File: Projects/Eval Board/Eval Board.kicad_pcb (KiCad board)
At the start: 2 copper layers, 50.8 x 33.5 mm, 34 parts, among them J1 I OUT, J2 Q OUT, J3 LO, J4 RF, U1 LTC5584

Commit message: Version 2
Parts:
- added J6: Conn_01x02, Connector_PinHeader_1.00mm:PinHeader_1x02_P1.00mm_Vertical, F.Cu at (175.9, 70.1)
- added J7: Conn_01x04, Connector_PinHeader_1.00mm:PinHeader_1x04_P1.00mm_Vertical, F.Cu at (200.7, 86.9)
- added J8: Conn_01x05, Connector_PinHeader_1.00mm:PinHeader_1x05_P1.00mm_Vertical, F.Cu at (182.9, 74.2)
- J1: value I OUT -> LO; footprint Kevin Library:SAMTEC_SMA-J-P-H-ST-EM1 -> AdditionalLibs:SAMTEC_SMA-J-P-H-ST-EM1
- J2: footprint Kevin Library:SAMTEC_SMA-J-P-H-ST-EM1 -> AdditionalLibs:SAMTEC_SMA-J-P-H-ST-EM1
- J3: value LO -> I Out; footprint Kevin Library:SAMTEC_SMA-J-P-H-ST-EM1 -> AdditionalLibs:SAMTEC_SMA-J-P-H-ST-EM1
- J4: value RF -> Q OUT; footprint Kevin Library:SAMTEC_SMA-J-P-H-ST-EM1 -> AdditionalLibs:SAMTEC_SMA-J-P-H-ST-EM1
- moved J1 32.7 mm to (217.6, 82.5), turned to 90 degrees
- moved J3 31.1 mm to (193.5, 67.3), turned to 180 degrees
- moved C21 18.4 mm to (196.6, 75.7), turned to 0 degrees
- moved C30 12.2 mm to (208.5, 75.7), turned to 0 degrees
- moved R14 5.77 mm to (206.8, 73.4)
- moved C35 5.39 mm to (183.9, 80.3), turned to 0 degrees
- moved C29 4.81 mm to (186.7, 73.7), turned to 180 degrees
- moved R9 4.67 mm to (190.0, 73.7)
- moved C41 4.34 mm to (191.0, 85.1)
- moved C19 4.06 mm to (182.9, 84.3)
- moved J2 3.86 mm to (207.0, 67.3)
- moved C31 3.07 mm to (193.0, 79.0)
- moved TR2 2.81 mm to (186.4, 84.8)
- moved L5 2.75 mm to (210.6, 82.5)
- moved C17 2.65 mm to (178.1, 84.3)
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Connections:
- net DCOI renamed /DCOI
- net DCOQ renamed /DCOQ
- net IP2I renamed /IP21
- net IP2Q renamed /IP2Q
- net Net-(C17-Pad1) renamed /RF
- net Net-(J2-Pad1) renamed /Q+
- net Net-(J2-Pad2_1) renamed /Q-
- C14 pad 1: Net-(C14-Pad1) -> /LO
- J1 pad 1: Net-(J1-Pad1) -> /LO
- J1 pad 2_1: Net-(J1-Pad2_1) -> GND
- J1 pad 2_2: Net-(J1-Pad2_1) -> GND
- J1 pad 3_1: Net-(J1-Pad2_1) -> GND
- J1 pad 3_2: Net-(J1-Pad2_1) -> GND
- J3 pad 1: Net-(C14-Pad1) -> /I+
- J3 pad 2_1: GND -> /I-
- J3 pad 2_2: GND -> /I-
- J3 pad 3_1: GND -> /I-
- J3 pad 3_2: GND -> /I-
- L5 pad 2: Net-(C14-Pad1) -> /LO
- R11 pad 1: Net-(J1-Pad1) -> /I+
- R9 pad 1: Net-(J1-Pad2_1) -> /I-
- U1 pad 22: Net-(J1-Pad1) -> /I+
- U1 pad 23: Net-(J1-Pad2_1) -> /I-
- U1 pad 25: (no net) -> GND
- U1 pad 9: Net-(U1-Pad9) -> Vbias
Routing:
- net GND: track 61.1 -> 10.5 mm, vias 169 -> 161
- net VCC: track 99.5 -> 61.3 mm, vias 4 -> 8
- net Net-(J1-Pad1): track 23.1 -> 0.00 mm
- net Net-(J1-Pad2_1): track 22.8 -> 0.00 mm, vias 18 -> 0
- net /I-: track 0.00 -> 13.4 mm, vias 0 -> 8
- net /I+: track 0.00 -> 12.6 mm
- net Net-(C14-Pad1): track 12.2 -> 0.00 mm
- net EN: track 0.00 -> 11.3 mm
- net Vbias: track 0.00 -> 10.5 mm
- net /Q+: track 25.7 -> 19.1 mm
- net /LO: track 0.00 -> 6.20 mm
- net EDC: track 0.00 -> 5.97 mm
- net /Q-: track 27.6 -> 21.6 mm, vias 40 -> 8
- net EIP2: track 0.00 -> 4.80 mm
- net /DCOI: track 10.1 -> 13.3 mm, vias 1 -> 0
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- added copper zone on B.Cu, net /I-
- added copper zone on F.Cu, net /I-
- added copper zone on B.Cu, net VCC
- removed copper zone on B.Cu, net Net-(J1-Pad2_1)
- removed copper zone on F.Cu, net Net-(J1-Pad2_1)
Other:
- board size 50.8 x 33.5 mm -> 48.3 x 27.3 mm
- board text removed: "GTRF Mixer Eval Board Rev 0.1"

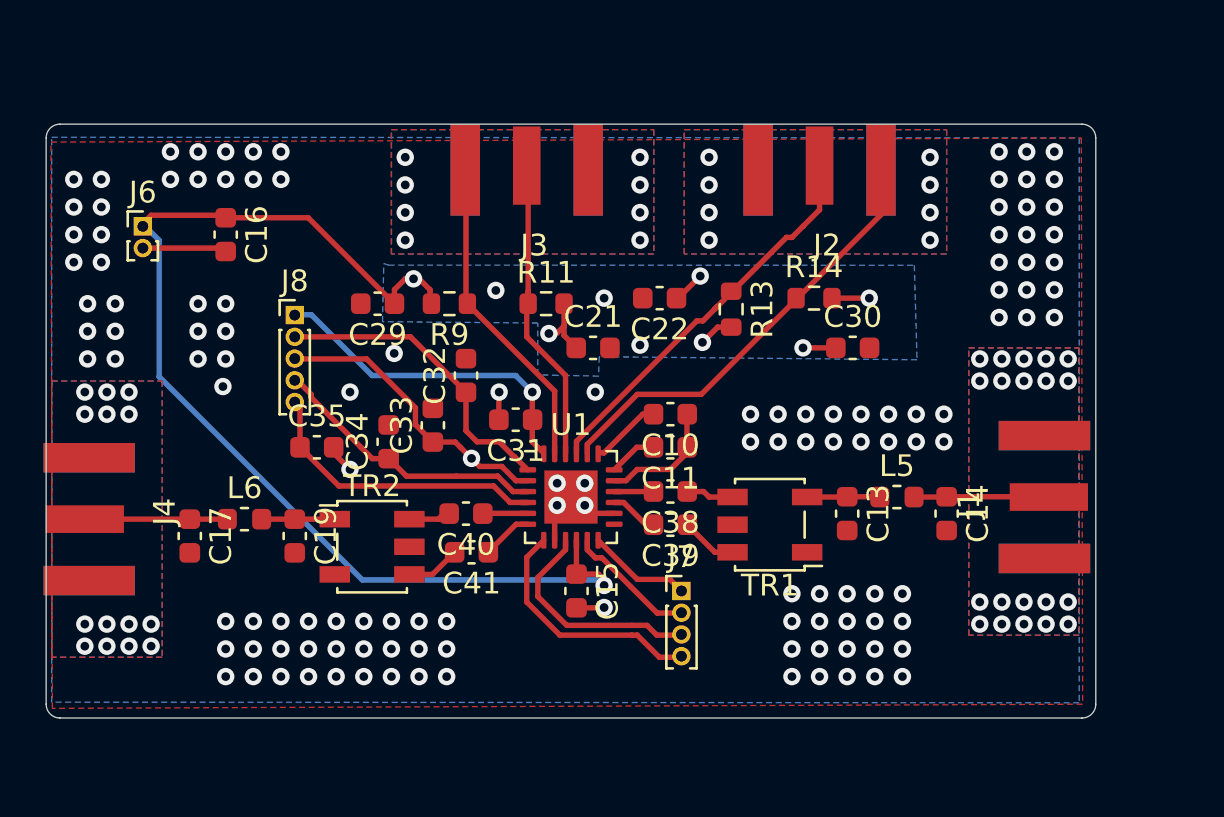
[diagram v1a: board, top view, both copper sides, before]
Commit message: Adjusted the VCC trace on the mixer eval board
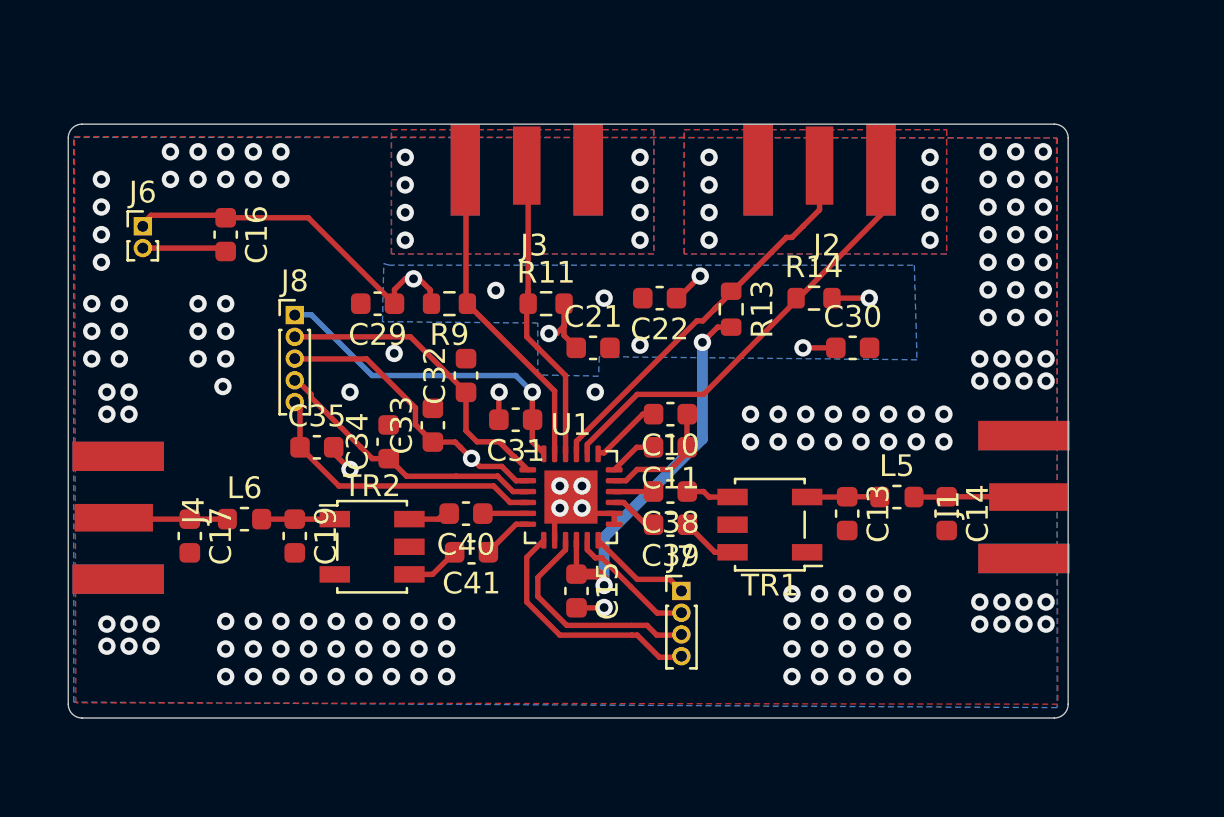
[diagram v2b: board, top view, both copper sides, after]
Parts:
- moved J4 1.34 mm to (174.6, 83.5)
- moved J1 0.94 mm to (216.6, 82.5)
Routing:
- net VCC: track 61.3 -> 42.8 mm
- net GND: track 10.5 -> 11.0 mm, vias 161 -> 149
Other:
- board size 48.3 x 27.3 mm -> 46 x 27.3 mm

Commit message: I made a 4 layer variant of the mixer PCB
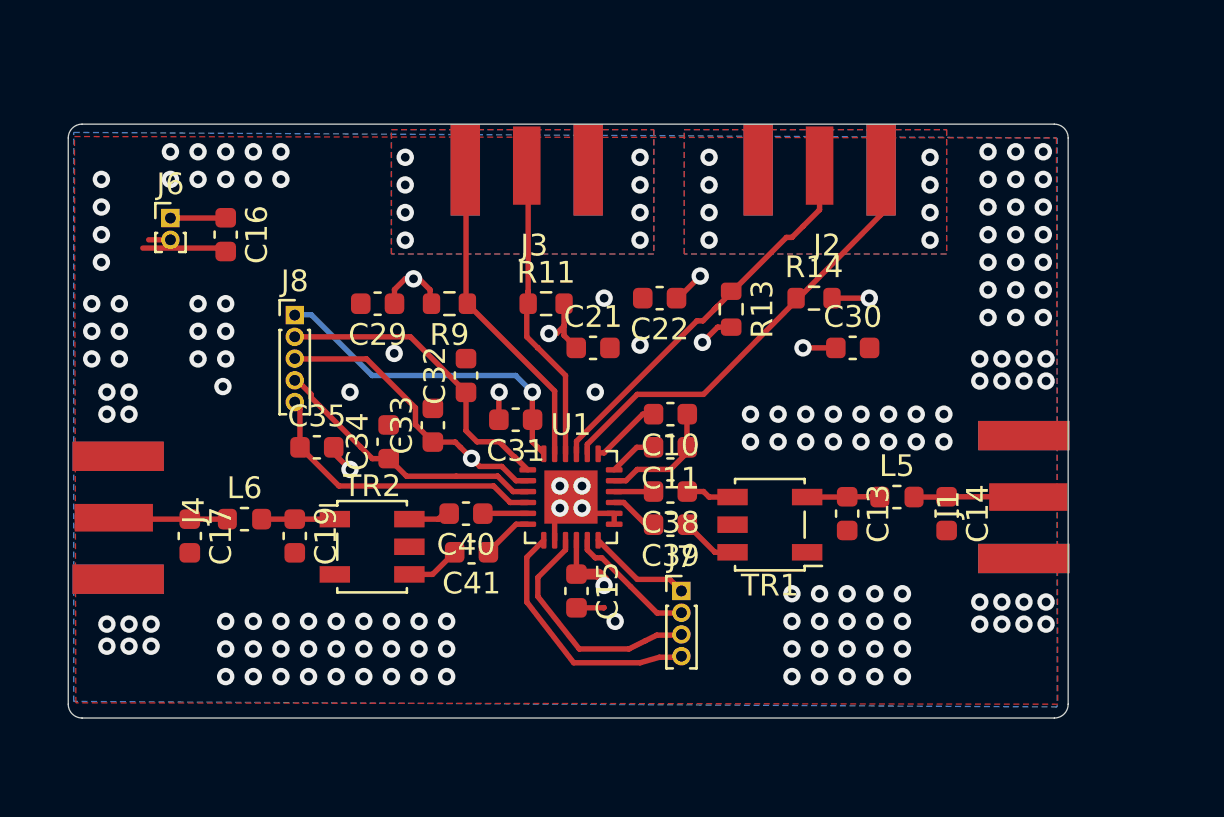
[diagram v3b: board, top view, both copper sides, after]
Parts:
- moved J6 1.33 mm to (177.2, 69.7)
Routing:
- net VCC: track 42.8 -> 19.0 mm, vias 8 -> 7
- net GND: track 11.0 -> 12.0 mm
- net Vbias: track 10.5 -> 11.0 mm
- added copper zone on In1.Cu, net GND
- added copper zone on In2.Cu, net VCC
- removed copper zone on B.Cu, net VCC
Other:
- copper layers 2 -> 4
- rule via_min_drill: 0.3 -> 0.2
- rule via_min_size: 0.4 -> 0.3

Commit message: Fixed DRC error on the jumpers
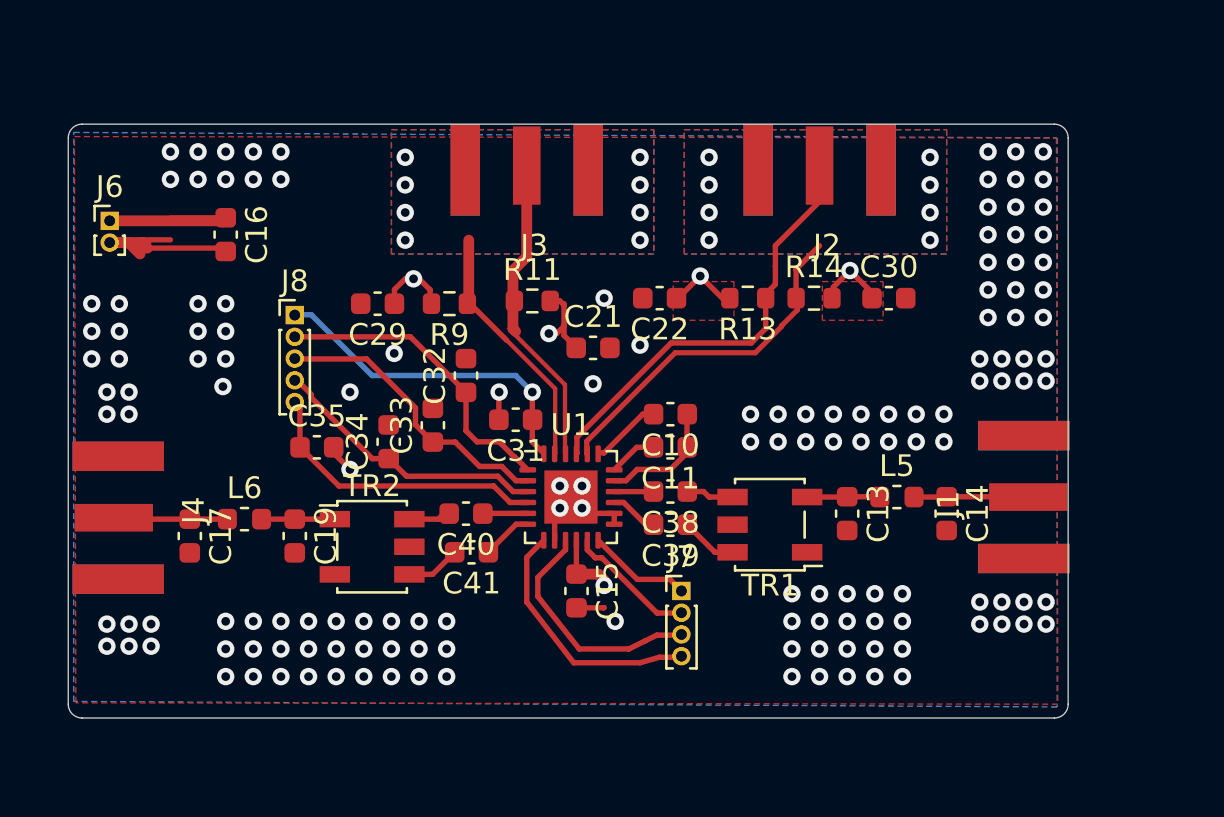
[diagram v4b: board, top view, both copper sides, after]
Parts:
- moved C30 2.83 mm to (210.2, 73.4)
- moved J6 2.80 mm to (174.4, 69.8)
- moved R13 0.92 mm to (203.7, 73.4), turned to 180 degrees
- moved R11 0.65 mm to (193.8, 73.5)
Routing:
- net VCC: track 19.0 -> 25.4 mm, vias 7 -> 5
- net /Q-: track 21.7 -> 16.2 mm
- net GND: track 12.0 -> 15.6 mm, vias 149 -> 145
- net /I-: track 13.4 -> 11.5 mm
- net /I+: track 12.6 -> 14.5 mm
- net /Q+: track 19.1 -> 20.3 mm
- net /DCOQ: vias 1 -> 0
- added copper zone on F.Cu, net VCC

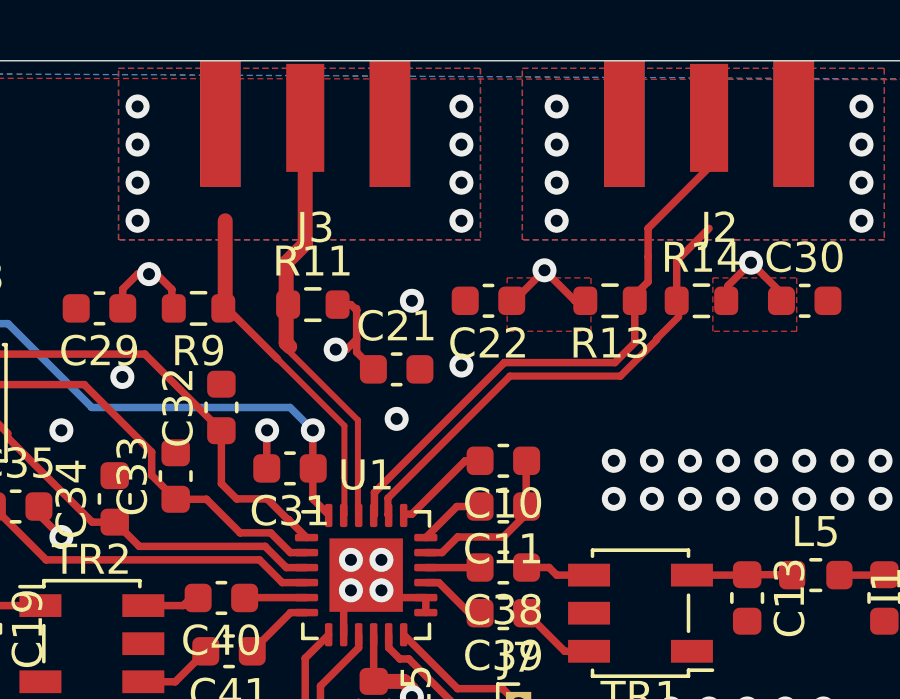
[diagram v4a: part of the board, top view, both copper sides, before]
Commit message: I tried to route diff pairs a little better on this one but they're still not good
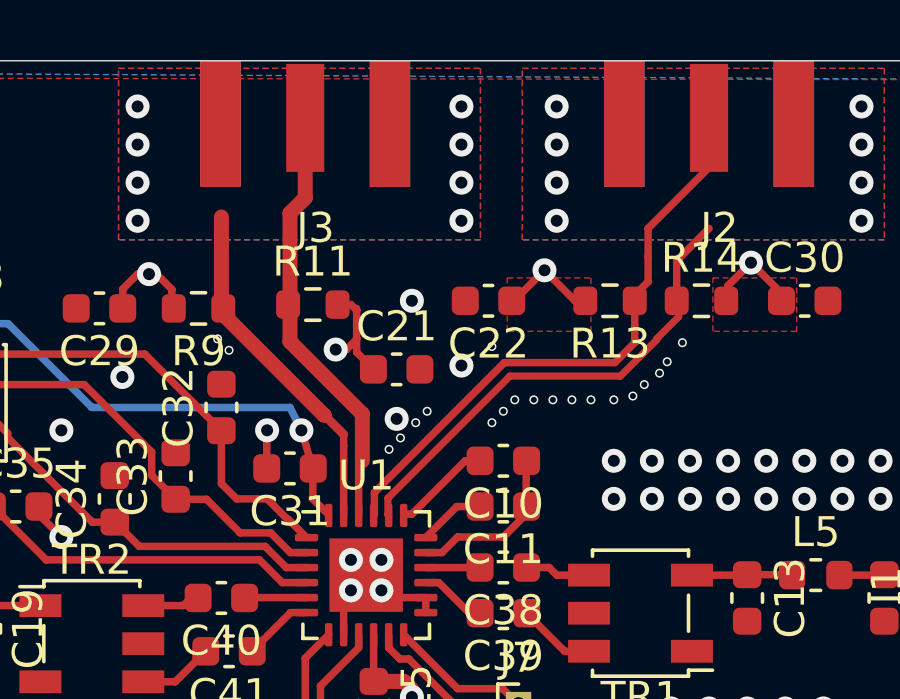
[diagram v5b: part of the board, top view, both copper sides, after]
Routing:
- net /I+: track 14.5 -> 15.3 mm
- net GND: vias 145 -> 165
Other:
- net class Dpair added: clearance 0.2, trace_width 0.25, via_dia 0.8, via_drill 0.4

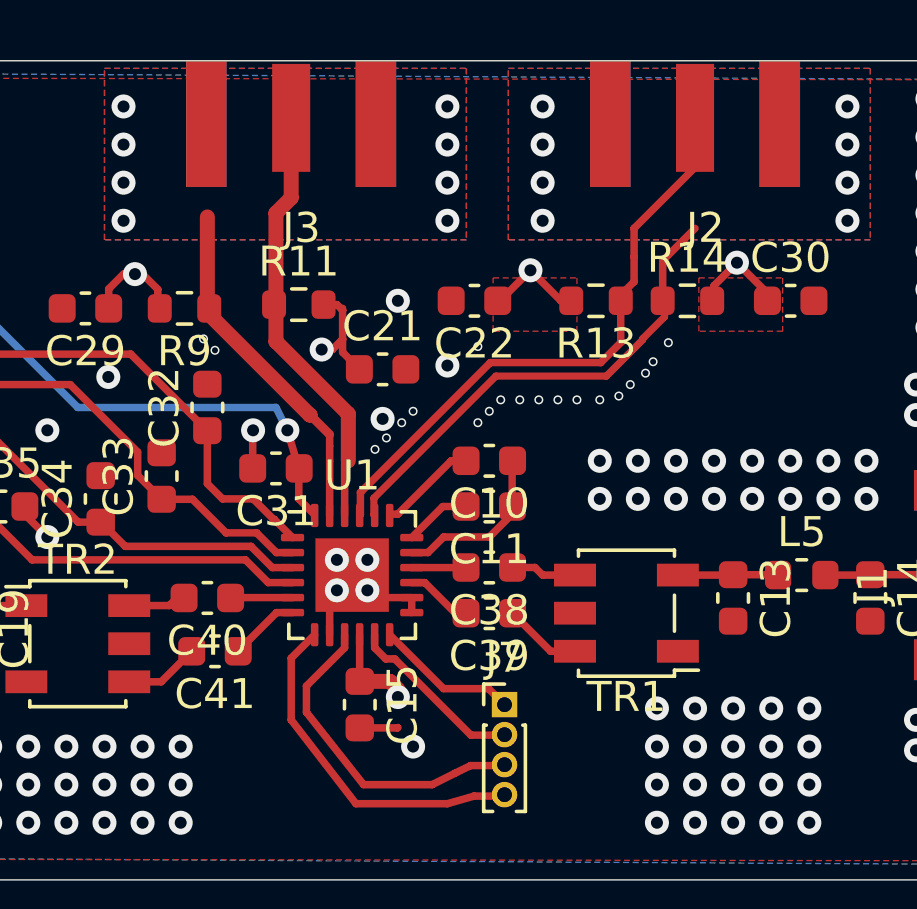
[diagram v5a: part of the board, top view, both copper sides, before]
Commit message: adjusted trace width on I+/- and Q+/- to reduce inductance. The traces are not drawn as duplex
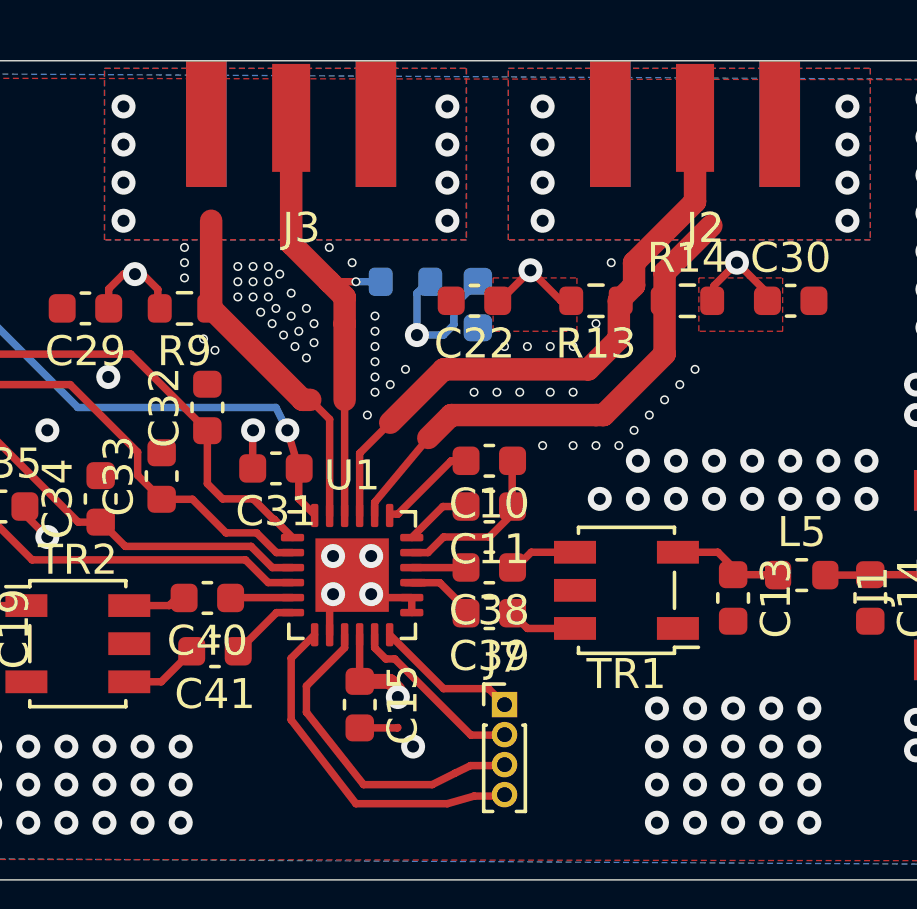
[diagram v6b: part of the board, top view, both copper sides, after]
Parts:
- C21, R11: moved to B.Cu
- moved C21 3.84 mm to (199.8, 73.5), turned to 270 degrees
- moved R11 3.64 mm to (197.4, 72.8)
- moved TR1 0.76 mm to (204.7, 83.1)
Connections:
- net Net-(C38-Pad1) renamed /LO+
- net Net-(C39-Pad1) renamed /LO-
- net Net-(C40-Pad2) renamed /RF+
- net Net-(C41-Pad2) renamed /RF-
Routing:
- net VCC: track 25.4 -> 26.6 mm
- net Net-(C39-Pad2): track 2.24 -> 3.32 mm
- net /Q-: track 16.2 -> 17.2 mm
- net /I+: track 15.3 -> 16.1 mm, vias 0 -> 1
- net /Q+: track 20.3 -> 21.0 mm
- net Net-(C13-Pad1): track 3.35 -> 3.87 mm
- net GND: vias 165 -> 199
